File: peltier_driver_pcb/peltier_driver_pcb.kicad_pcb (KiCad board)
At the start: 2 copper layers, 35 x 52 mm, 20 parts, among them J1 Conn_01x04, J2 Pt1000_top, J3 Peltier_A, J4 Peltier_B, U1 MCP601-xSN, U2 OLED_128x32_I2C, U3 INA260, U4 LM334Z

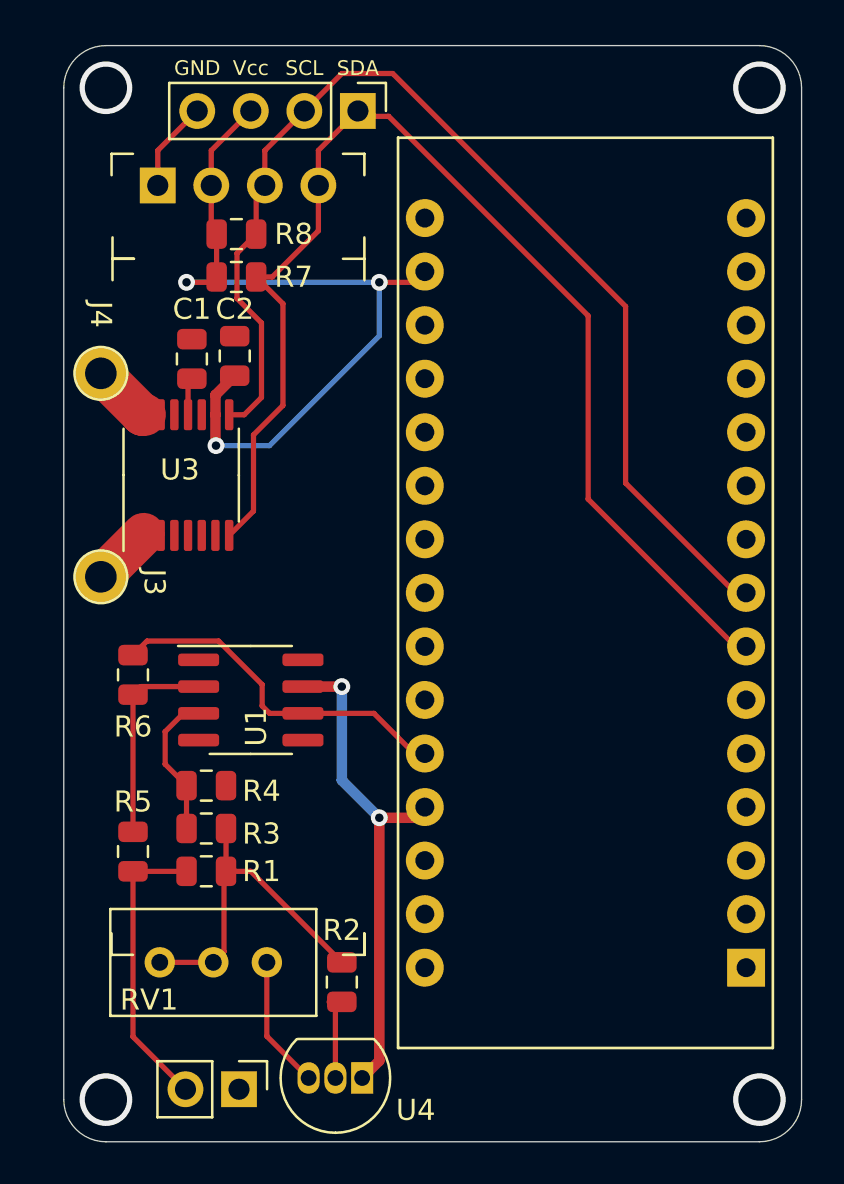
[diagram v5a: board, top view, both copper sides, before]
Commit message: resettable fuse, rearranged board for neatness
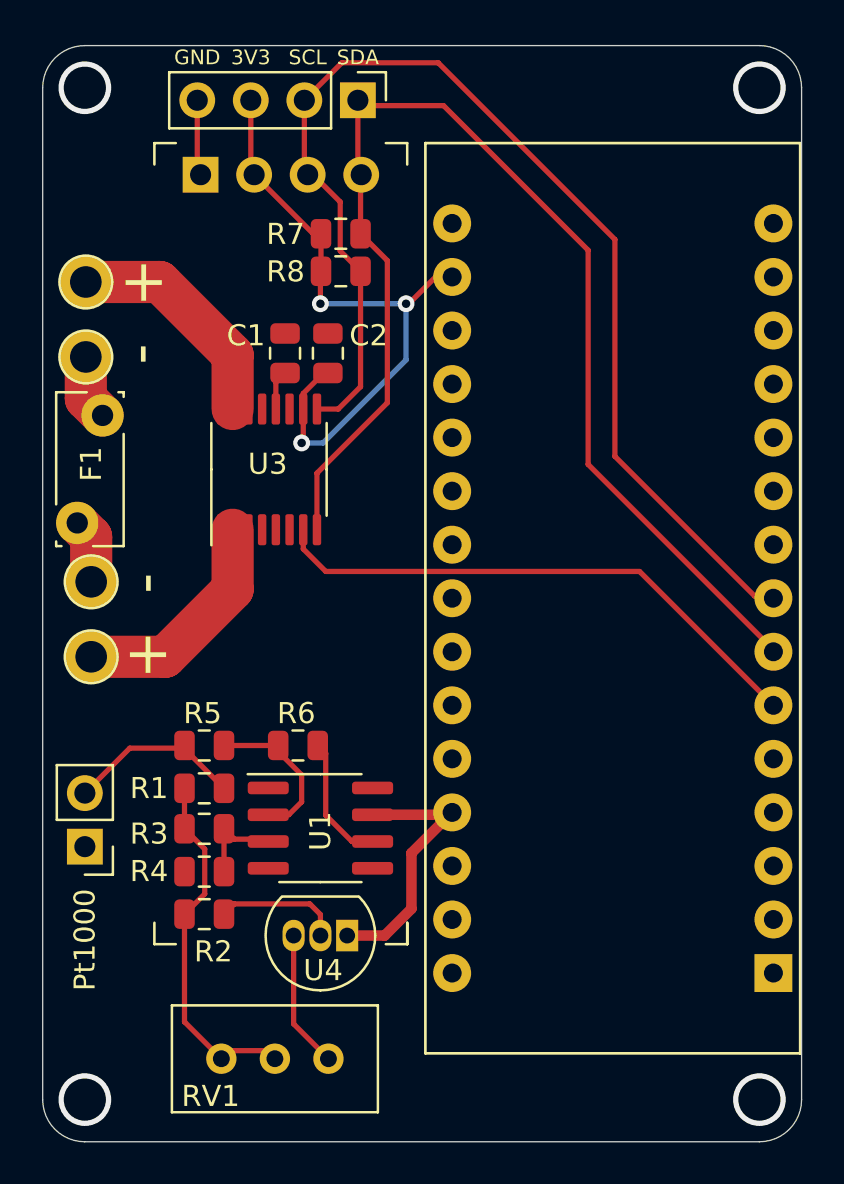
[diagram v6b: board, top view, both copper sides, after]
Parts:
- added F1: 3A hold, 5.1A trip, Fuse:Fuse_Bourns_MF-RG300, F.Cu at (110.6, 73.6)
- added J5: Peltier_1a, Connector_Pin:Pin_D1.0mm_L10.0mm, F.Cu at (111.0, 65.8)
- added J6: Peltier_2a, Connector_Pin:Pin_D1.0mm_L10.0mm, F.Cu at (111.3, 76.4)
- J3: value Peltier_A -> Peltier_1b
- J4: value Peltier_B -> Peltier_2b
- moved J2 13.6 mm to (111.0, 89.0), turned to 180 degrees
- moved R6 8.51 mm to (121.1, 84.2), turned to 180 degrees
- moved R2 7.28 mm to (116.7, 92.2), turned to 0 degrees
- moved U1 6.92 mm to (122.2, 88.1)
- moved U4 6.79 mm to (123.4, 93.2)
- moved R5 6.06 mm to (116.7, 84.2), turned to 180 degrees
- moved RV1 5.43 mm to (122.6, 99.1)
- moved R7 5.36 mm to (123.1, 59.9)
- moved R8 5.26 mm to (123.1, 61.7)
- moved C1 4.43 mm to (120.5, 65.6)
- moved C2 4.42 mm to (122.5, 65.6)
- moved J4 4.39 mm to (111.0, 62.2)
- moved U3 4.17 mm to (119.7, 71.1)
- moved R4 4.08 mm to (116.7, 90.2), turned to 180 degrees
- moved R1 3.94 mm to (116.7, 86.2), turned to 0 degrees
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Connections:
- TB1 pad 6: Net-(TB1-Pad6) -> ALRT
- U3 pad 7: Net-(U3-Pad7) -> ALRT
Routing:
- net ALRT: track 0.00 -> 26.3 mm
- net T_sense: track 17.9 -> 6.26 mm
- net +5V: track 23.9 -> 12.8 mm, vias 2 -> 0
- net IN-: track 2.90 -> 11.0 mm
- net IN+: track 2.87 -> 10.9 mm
- net +3V3: track 38.0 -> 31.6 mm
- net Net-(J2-Pad2): track 14.5 -> 8.47 mm
- net Net-(F1-Pad2): track 0.00 -> 3.10 mm
- net Net-(F1-Pad1): track 0.00 -> 3.07 mm
- net Net-(R3-Pad2): track 6.96 -> 4.72 mm
- net Net-(R5-Pad1): track 9.78 -> 7.55 mm
- net SCL: track 54.4 -> 56.3 mm
- net Net-(R2-Pad2): track 4.34 -> 5.98 mm
- net GND: track 4.44 -> 3.60 mm
- net SDA: track 58.4 -> 59.0 mm
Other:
- board size 35 x 52 mm -> 36 x 52 mm
- board text added: "+"
- board text added: "-"
- board text added: "Pt1000"

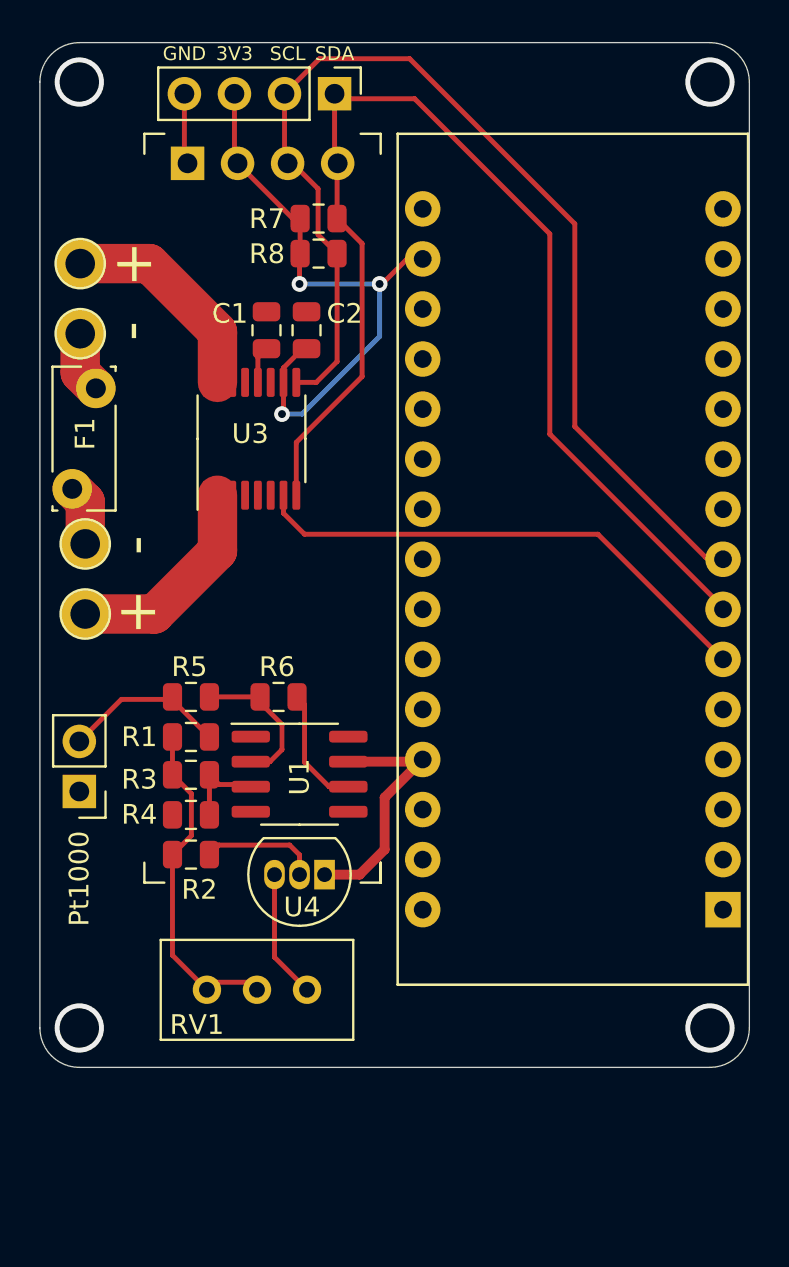
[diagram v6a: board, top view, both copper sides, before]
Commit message: added break-out for remaining Arduino pins
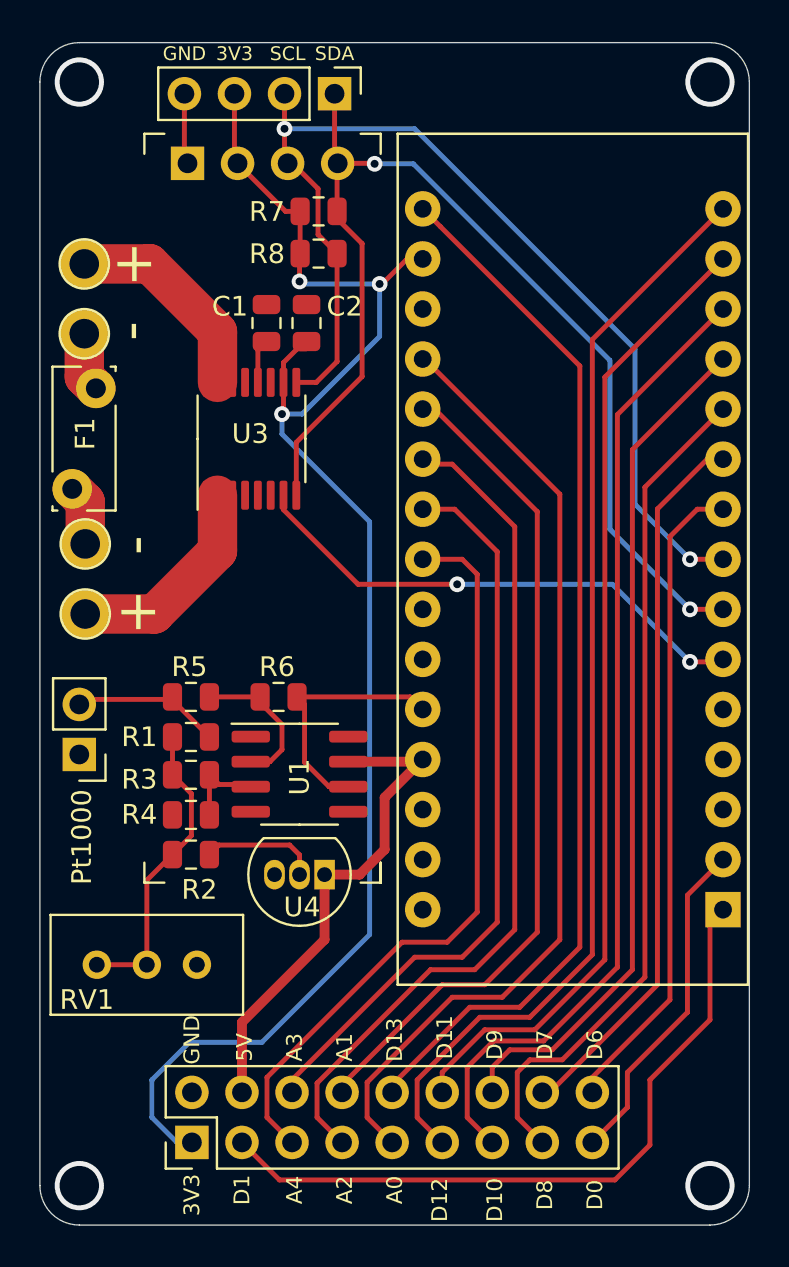
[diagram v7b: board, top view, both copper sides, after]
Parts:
- added J7: Arduino_breakout, Connector_PinHeader_2.54mm:PinHeader_2x09_P2.54mm_Vertical, F.Cu at (116.7, 106.8)
- moved RV1 5.73 mm to (117.0, 97.8)
- moved J2 1.88 mm to (111.0, 87.1)
- moved C1 0.36 mm to (120.5, 65.2)
- moved C2 0.36 mm to (122.5, 65.2)
- moved R7 0.36 mm to (123.1, 59.6)
- moved J4 0.21 mm to (111.3, 62.2)
- moved J5 0.21 mm to (111.3, 65.8)
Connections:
- net Net-(TB1-Pad24) renamed POT_fine
- net Net-(TB1-Pad25) renamed POT_coarse
- net Net-(TB1-Pad5) renamed BTN
- TB1 pad 1: Net-(TB1-Pad1) -> D1
- TB1 pad 10: Net-(TB1-Pad10) -> D7
- TB1 pad 11: Net-(TB1-Pad11) -> D8
- TB1 pad 12: Net-(TB1-Pad12) -> D9
- TB1 pad 13: Net-(TB1-Pad13) -> D10
- TB1 pad 14: Net-(TB1-Pad14) -> D11
- TB1 pad 15: Net-(TB1-Pad15) -> D12
- TB1 pad 16: Net-(TB1-Pad16) -> D13
- TB1 pad 19: Net-(TB1-Pad19) -> A0
- TB1 pad 2: Net-(TB1-Pad2) -> D0
- TB1 pad 20: Net-(TB1-Pad20) -> A1
- TB1 pad 21: Net-(TB1-Pad21) -> A2
- TB1 pad 22: Net-(TB1-Pad22) -> A3
- TB1 pad 23: Net-(TB1-Pad23) -> A4
- TB1 pad 9: Net-(TB1-Pad9) -> D6
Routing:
- net D12: track 0.00 -> 55.8 mm
- net D13: track 0.00 -> 53.6 mm
- net D10: track 0.00 -> 49.7 mm
- net D11: track 0.00 -> 49.7 mm
- net A0: track 0.00 -> 48.8 mm
- net +3V3: track 31.6 -> 79.0 mm
- net A2: track 0.00 -> 43.3 mm
- net D9: track 0.00 -> 43.3 mm
- net D8: track 0.00 -> 43.0 mm
- net A1: track 0.00 -> 42.8 mm
- net A4: track 0.00 -> 38.2 mm
- net A3: track 0.00 -> 37.8 mm
- net D7: track 0.00 -> 36.6 mm
- net D1: track 0.00 -> 35.7 mm
- net D6: track 0.00 -> 33.1 mm
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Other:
- board size 36 x 52 mm -> 36 x 60 mm
- board text added: "3V3"
- board text added: "5V"
- board text added: "A0"
- board text added: "A1"
- board text added: "A2"
- board text added: "A3"
- board text added: "A4"
- board text added: "D0"
- board text added: "D1"
- board text added: "D10"
- board text added: "D11"
- board text added: "D12"
- board text added: "D13"
- board text added: "D6"
- board text added: "D7"
- board text added: "D8"
- board text added: "D9"
- board text added: "GND"

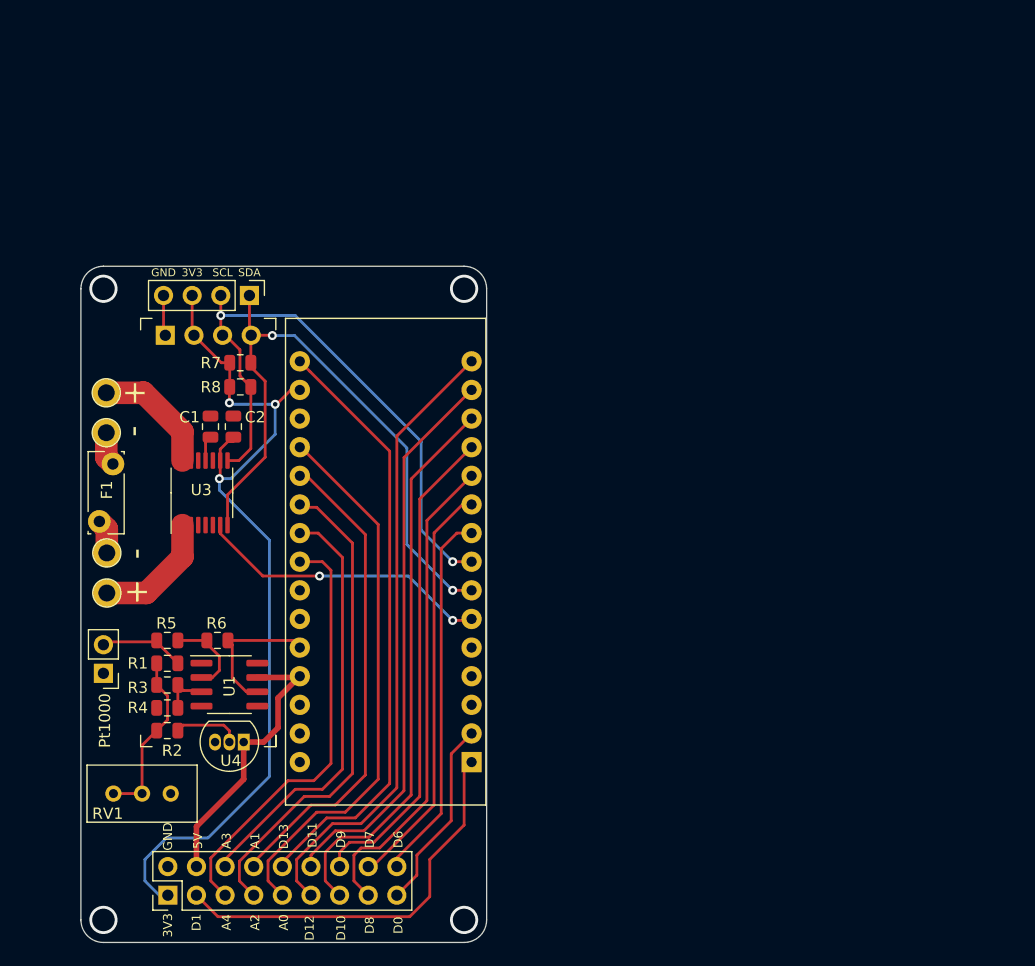
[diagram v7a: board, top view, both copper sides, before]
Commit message: ltspice sims and modular pcb v1
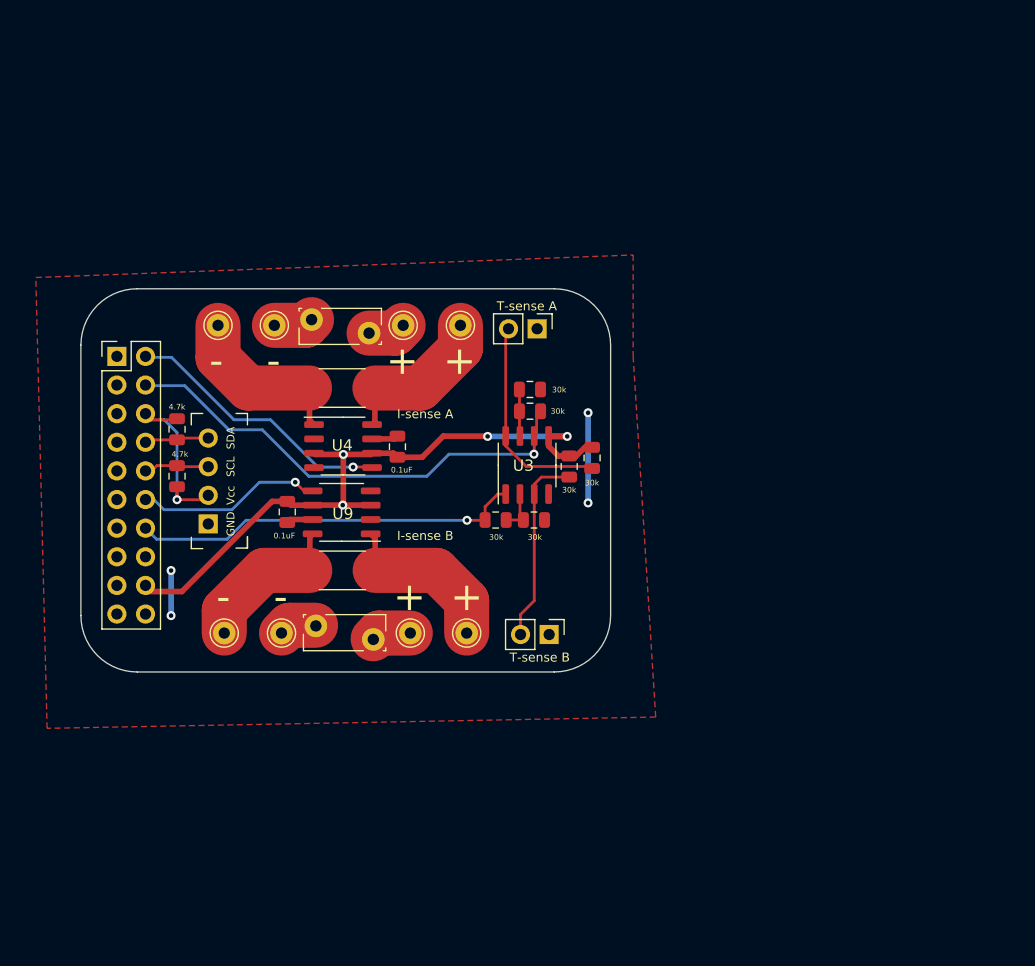
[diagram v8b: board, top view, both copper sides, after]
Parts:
- removed C2: 0.1uF, Capacitor_SMD:C_0805_2012Metric
- removed J6: Peltier_2a, Connector_Pin:Pin_D1.0mm_L10.0mm
- removed J7: Arduino_breakout, Connector_PinHeader_2.54mm:PinHeader_2x09_P2.54mm_Vertical
- removed RV1: 3K, Potentiometer_THT:Potentiometer_Bourns_3296W_Vertical
- removed TB1: ARDUINO_NANO, ARDUINO_NANO:SHIELD_ARDUINO_NANO
- removed U2: OLED_128x32_I2C, peltier_driver_pcb:OLED_128x32_I2C
- added C6: 0.1uF, Capacitor_SMD:C_0805_2012Metric, F.Cu at (127.3, 72.8)
- added F6: 3A hold, 5.1A trip, Fuse:Fuse_Bourns_MF-RG300, F.Cu at (129.8, 82.9)
- added J10: GA10K4A1_NTC, Connector_PinHeader_2.54mm:PinHeader_1x02_P2.54mm_Vertical, F.Cu at (149.5, 56.5)
- added J21: Peltier V-, Connector_Pin:Pin_D1.0mm_L10.0mm, F.Cu at (138.2, 83.5)
- added J22: Driver V-, Connector_Pin:Pin_D1.0mm_L10.0mm, F.Cu at (126.8, 83.5)
- added J25: Peltier V+, Connector_Pin:Pin_D1.0mm_L10.0mm, F.Cu at (143.2, 83.5)
- added J28: Driver V+, Connector_Pin:Pin_D1.0mm_L10.0mm, F.Cu at (121.7, 83.5)
- added J9: Conn_02x10_Top_Bottom, Connector_PinHeader_2.54mm:PinHeader_2x10_P2.54mm_Vertical, F.Cu at (112.2, 59.0)
- added R14: 0.5m, Resistor_SMD:R_2512_6332Metric, F.Cu at (132.2, 78.0)
- added R9: 30K, Resistor_SMD:R_0805_2012Metric, F.Cu at (154.4, 68.0)
- added U9: INA283, Package_SO:SO-8_3.9x4.9mm_P1.27mm, F.Cu at (132.1, 72.8)
- C1: value C_BUS -> 0.1uF
- J1: value Conn_01x04 -> Peltier V-; footprint Connector_PinHeader_2.54mm:PinHeader_1x04_P2.54mm_Vertical -> Connector_Pin:Pin_D1.0mm_L10.0mm
- J2: value Pt1000_top -> Driver V-; footprint Connector_PinHeader_2.54mm:PinHeader_1x02_P2.54mm_Vertical -> Connector_Pin:Pin_D1.0mm_L10.0mm
- J3: value Peltier_1b -> GA10K4A1_NTC; footprint Connector_Pin:Pin_D1.0mm_L10.0mm -> Connector_PinHeader_2.54mm:PinHeader_1x02_P2.54mm_Vertical
- J4: value Peltier_2b -> Peltier V+
- J5: value Peltier_1a -> Driver V+
- R1, R2: value 1K -> 4.7k
- R3, R4: value 1K -> 30K
- R5: value 100k -> 30K
- R6: value 100k -> 0.5m; footprint Resistor_SMD:R_0805_2012Metric -> Resistor_SMD:R_2512_6332Metric
- R7, R8: value 4K7 -> 30K
- U1: value MCP601-xSN -> OLED_128x32_I2C; footprint Package_SO:SOIC-8_3.9x4.9mm_P1.27mm -> peltier_driver_pcb:OLED_128x32_I2C
- U3: value INA260 -> MCP602; footprint Package_SO:TSSOP-16_4.4x5mm_P0.65mm -> Package_SO:SO-8_3.9x4.9mm_P1.27mm
- U4: value LM334Z -> INA283; footprint Package_TO_SOT_THT:TO-92_Inline -> Package_SO:SO-8_3.9x4.9mm_P1.27mm
- moved R3 40.6 mm to (152.3, 68.8), turned to 90 degrees
- moved J3 39.4 mm to (150.5, 83.7), turned to 270 degrees
- moved J2 34.4 mm to (126.2, 56.2), turned to 0 degrees
- moved R5 34.2 mm to (149.2, 73.5), turned to 0 degrees
- moved R4 33.6 mm to (145.8, 73.5), turned to 0 degrees
- moved J5 32.8 mm to (142.7, 56.2)
- moved U3 29.0 mm to (148.6, 68.6)
- moved U4 27.7 mm to (132.3, 67.0), turned to 0 degrees
- moved R2 26.7 mm to (117.5, 65.5), turned to 270 degrees
- moved R7 26.1 mm to (148.8, 63.9), turned to 180 degrees
- moved F1 26.0 mm to (129.5, 55.7), turned to 0 degrees
- moved R8 25.7 mm to (148.8, 61.9)
- moved R6 25.0 mm to (132.2, 61.8)
- moved C1 16.7 mm to (137.1, 67.0), turned to 270 degrees
- moved R1 16.6 mm to (117.5, 69.6), turned to 90 degrees
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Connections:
- C1 pad 1: Net-(C1-Pad1) -> GND
- C1 pad 2: GND -> +5V
- J1 pad 1: SDA -> Net-(F1-Pad2)
- J2 pad 1: GND -> Net-(F1-Pad1)
- J3 pad 1: IN+ -> GND
- J4 pad 1: IN- -> Net-(J4-Pad1)
- J5 pad 1: Net-(F1-Pad2) -> Net-(J5-Pad1)
- R1 pad 1: I_ref -> +3V3
- R1 pad 2: Net-(J2-Pad2) -> SCL
- R2 pad 1: I_ref -> +3V3
- R2 pad 2: Net-(R2-Pad2) -> SDA
- R3 pad 1: I_ref -> Net-(J3-Pad2)
- R3 pad 2: Net-(R3-Pad2) -> +5V
- R4 pad 1: Net-(R3-Pad2) -> T_sense1
- R4 pad 2: GND -> Net-(R4-Pad2)
- R5 pad 1: Net-(R5-Pad1) -> Net-(R4-Pad2)
- R5 pad 2: Net-(J2-Pad2) -> GND
- R6 pad 1: T_sense -> Net-(J5-Pad1)
- R6 pad 2: Net-(R5-Pad1) -> Net-(J4-Pad1)
- R7 pad 1: +3V3 -> T_sense2
- R7 pad 2: SDA -> Net-(R7-Pad2)
- R8 pad 1: +3V3 -> Net-(R7-Pad2)
- R8 pad 2: SCL -> GND
- U1 pad 1: Net-(U1-Pad1) -> GND
- U1 pad 2: Net-(R5-Pad1) -> +3V3
- U1 pad 3: Net-(R3-Pad2) -> SCL
- U1 pad 4: GND -> SDA
- U3 pad 1: IN+ -> T_sense1
- U3 pad 2: IN+ -> Net-(R4-Pad2)
- U3 pad 3: IN+ -> Net-(J3-Pad2)
- U3 pad 5: GND -> +5V
- U3 pad 6: GND -> T_sense2
- U3 pad 7: ALRT -> Net-(R7-Pad2)
- U3 pad 8: SDA -> Net-(J10-Pad2)
- U4 pad 1: +5V -> Net-(J4-Pad1)
- U4 pad 2: Net-(R2-Pad2) -> GND
- U4 pad 3: Net-(RV1-Pad1) -> +5V
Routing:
- net +3V3: track 79.0 -> 16.4 mm, vias 3 -> 1
- net D12: track 55.8 -> 0.00 mm
- net D13: track 53.6 -> 0.00 mm
- net SDA: track 57.4 -> 5.95 mm, vias 2 -> 0
- net D10: track 49.7 -> 0.00 mm
- net D11: track 49.7 -> 0.00 mm
- net A0: track 48.8 -> 0.00 mm
- net SCL: track 53.0 -> 6.02 mm, vias 2 -> 0
- net A2: track 43.3 -> 0.00 mm
- net D9: track 43.3 -> 0.00 mm
- net D8: track 43.0 -> 0.00 mm
- net T_sense2: track 0.00 -> 42.9 mm, vias 0 -> 1
- net A1: track 42.8 -> 0.00 mm
- net A4: track 38.2 -> 0.00 mm
- net A3: track 37.8 -> 0.00 mm
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- added copper zone on F.Cu, net GND
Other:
- board size 36 x 60 mm -> 47 x 34 mm
- net class Gnd added: clearance 0.2, trace_width 0.5, via_dia 0.8, via_drill 0.4
- board text added: "0.1uF"
- board text added: "30k"
- board text added: "4.7k"
- board text added: "I-sense A"
- board text added: "I-sense B"
- board text added: "T-sense A"
- board text added: "T-sense B"
- board text removed: "3V3"
- board text removed: "5V"
- board text removed: "A0"
- board text removed: "A1"
- board text removed: "A2"
- board text removed: "A3"
- board text removed: "A4"
- board text removed: "D0"
- board text removed: "D1"
- board text removed: "D10"
- board text removed: "D11"
- board text removed: "D12"
- board text removed: "D13"
- board text removed: "D6"
- board text removed: "D7"
- board text removed: "D8"
- board text removed: "D9"
- board text removed: "GND"
- board text removed: "Pt1000"
